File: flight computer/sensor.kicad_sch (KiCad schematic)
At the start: 131 parts, among them IC1 A3909, J1 Micro_SD_Card_Det1, J12 Conn_01x04, J13 1x3 servo, J14 1x3 servo, J15 arming terminal, J16 arming terminal, J17 H9161TR-ND, J19 Screw_Terminal_01x02, J20 Screw_Terminal_01x02, J3 H9161TR-ND, J4 H9161TR-ND, J5 Screw_Term, J6 1x3 servo, J9 1x3 servo, Q1 IRLML6402, Q3 IRLML6402, Q4 IRLML6402, Q5 IRLML6402, Q6 IRLML6402, Q7 BSS138, Q8 IRLML6402, Q9 IRLML6402, U10 LSM6DS3, U11 BGM220SC12WGA2R, U12 PE4259, U5 LPS22HB, U6 GPS, U7 SX1276, U8 NAND, Y4 32MHz

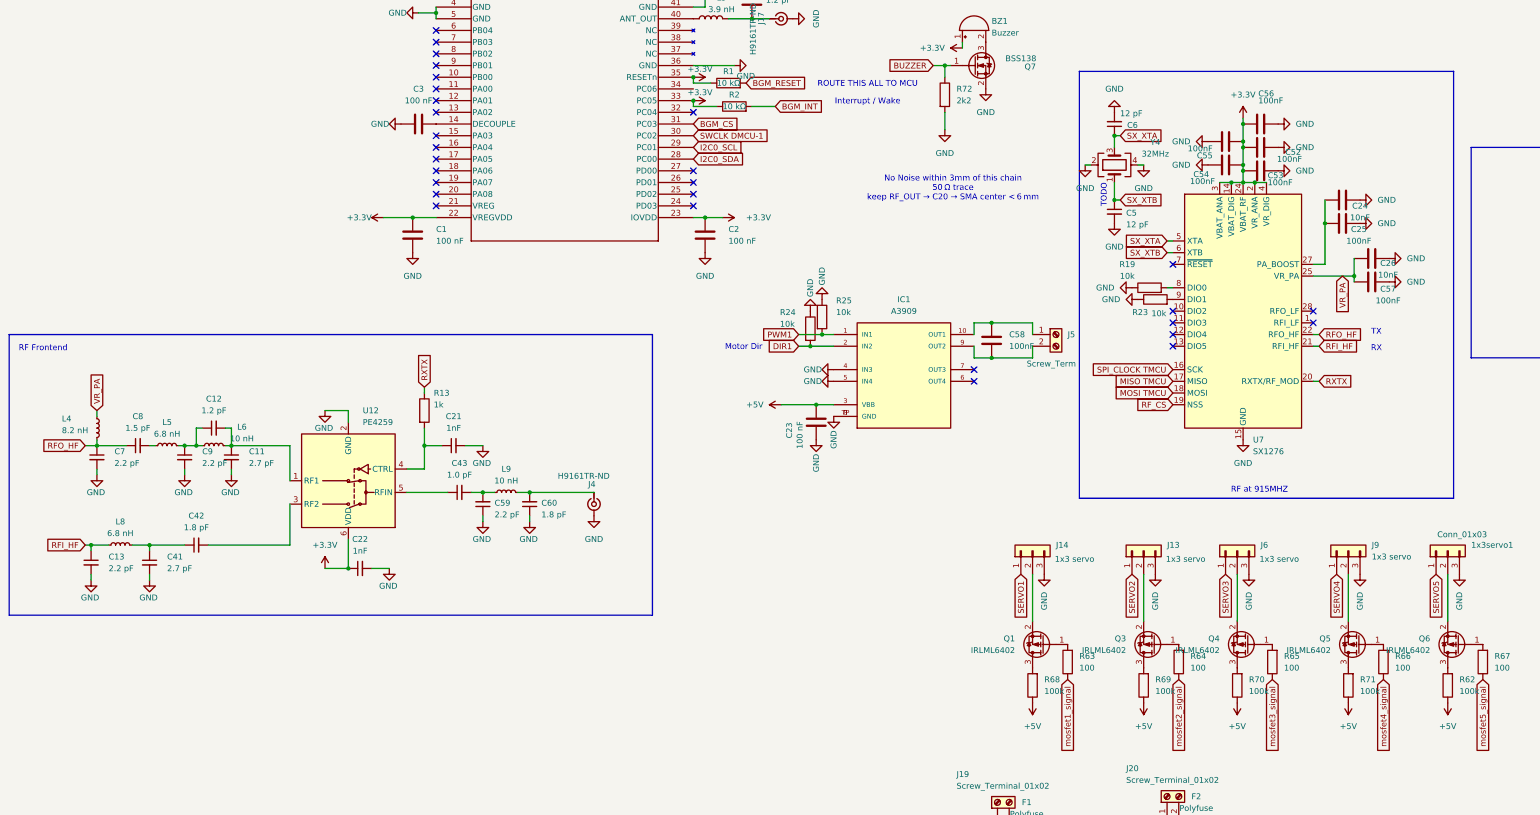
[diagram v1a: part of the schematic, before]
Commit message: Meddy, the PCB is ready for you. The proper RF is setup too on the PCB
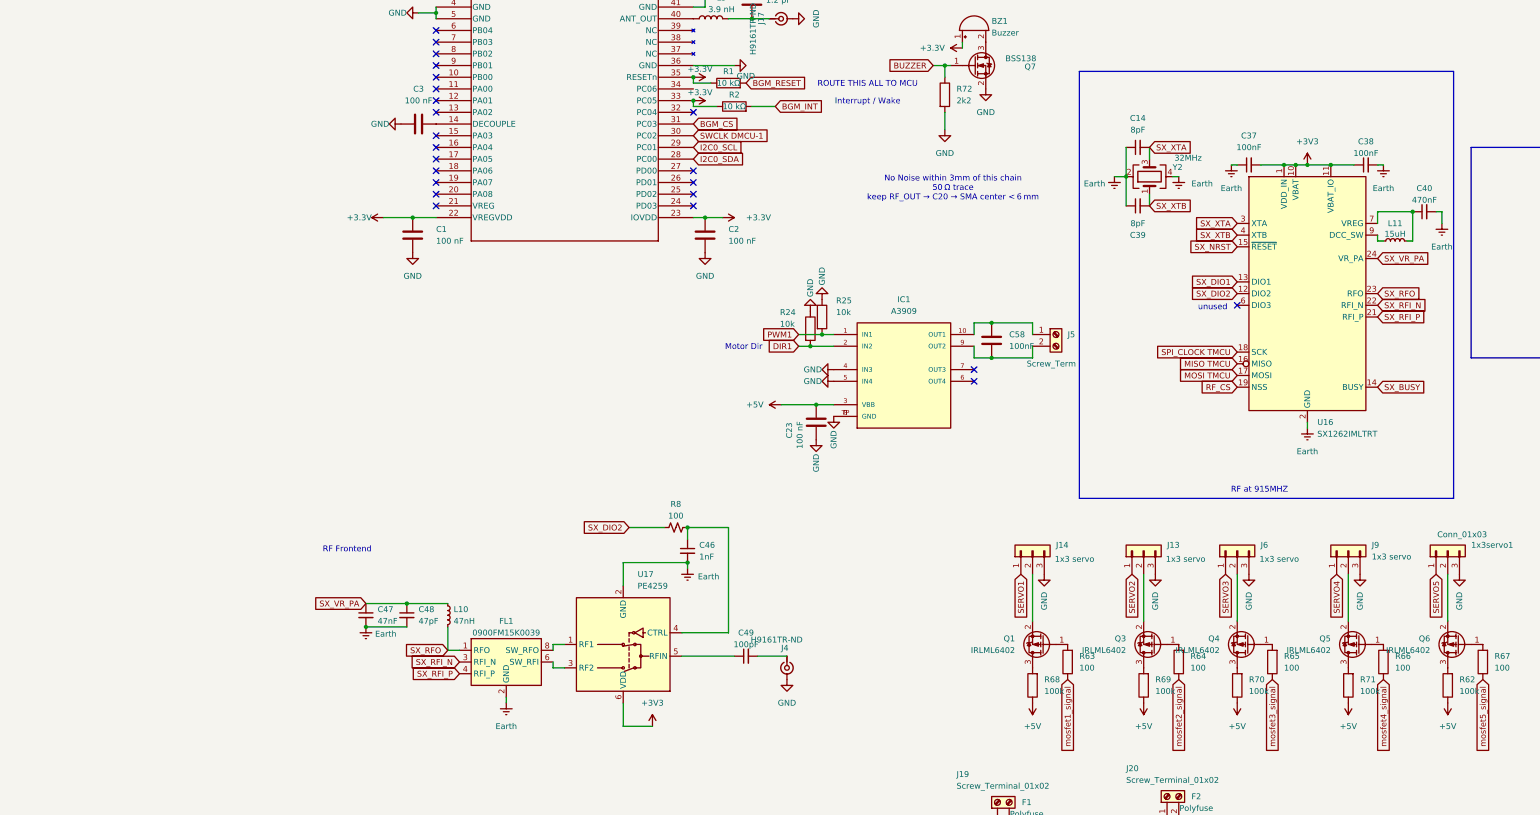
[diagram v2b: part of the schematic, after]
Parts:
- removed C11, C41: 2.7 pF, Capacitor_SMD:C_0603_1608Metric, symbol Device:C_Small
- removed C12: 1.2 pF, Capacitor_SMD:C_0603_1608Metric, symbol Device:C_Small
- removed C13, C59, C7, C9: 2.2 pF, Capacitor_SMD:C_0603_1608Metric, symbol Device:C_Small
- removed C21, C22: 1nF, Capacitor_SMD:C_0603_1608Metric, symbol Device:C_Small
- removed C24, C26: 10nF, Capacitor_SMD:C_0603_1608Metric, symbol Device:C
- removed C25, C52, C53, C54, C55, C56, C57: 100nF, Capacitor_SMD:C_0603_1608Metric, symbol Device:C
- removed C42, C60: 1.8 pF, Capacitor_SMD:C_0603_1608Metric, symbol Device:C_Small
- removed C43: 1.0 pF, Capacitor_SMD:C_0603_1608Metric, symbol Device:C_Small
- removed C5, C6: 12 pF, Capacitor_SMD:C_0603_1608Metric, symbol Device:C_Small
- removed C8: 1.5 pF, Capacitor_SMD:C_0603_1608Metric, symbol Device:C_Small
- removed L4: 8.2 nH, Inductor_SMD:L_0603_1608Metric, symbol Device:L_Small
- removed L5, L8: 6.8 nH, Inductor_SMD:L_0603_1608Metric, symbol Device:L_Small
- removed L6, L9: 10 nH, Inductor_SMD:L_0603_1608Metric, symbol Device:L_Small
- removed R13: 1k, Resistor_SMD:R_0603_1608Metric, symbol Device:R
- removed R19, R23: 10k, Resistor_SMD:R_0603_1608Metric, symbol Device:R
- removed U12: PE4259, Package_TO_SOT_SMD:SOT-363_SC-70-6, symbol RF_Switch:BGS12WN6E6327
- removed U7: SX1276, Package_DFN_QFN:QFN-28-1EP_6x6mm_P0.65mm_EP4.8x4.8mm, symbol RF:SX1276
- removed Y4: 32MHz, Crystal:Crystal_SMD_Abracon_ABM10-4Pin_2.5x2.0mm, symbol Device:Crystal_GND24
- added C14, C39: 8pF, Capacitor_SMD:C_0603_1608Metric, symbol Device:C_Small
- added C37, C38: 100nF, Capacitor_SMD:C_0603_1608Metric, symbol Device:C_Small
- added C40: 470nF, Capacitor_SMD:C_0603_1608Metric, symbol Device:C_Small
- added C46: 1nF, Capacitor_SMD:C_0603_1608Metric, symbol Device:C_Small
- added C47: 47nF, Capacitor_SMD:C_0603_1608Metric, symbol Device:C_Small
- added C48: 47pF, Capacitor_SMD:C_0603_1608Metric, symbol Device:C_Small
- added C49: 100pF, Capacitor_SMD:C_0603_1608Metric, symbol Device:C_Small
- added FL1: 0900FM15K0039, RF_Converter:Balun_Johanson_0900FM15K0039, symbol Filter:0900FM15K0039
- added L10: 47nH, Inductor_SMD:L_0603_1608Metric, symbol Device:L_Small
- added L11: 15uH, Inductor_SMD:L_0805_2012Metric, symbol Device:L_Small
- added R8: 100, Resistor_SMD:R_0603_1608Metric, symbol Device:R_Small_US
- added U16: SX1262IMLTRT, Package_DFN_QFN:QFN-24-1EP_4x4mm_P0.5mm_EP2.6x2.6mm, symbol RF:SX1262IMLTRT
- added U17: PE4259, Package_TO_SOT_SMD:SOT-363_SC-70-6, symbol RF_Switch_Extended:PE4259
- added Y2: 32MHz, Crystal:Crystal_SMD_3225-4Pin_3.2x2.5mm, symbol Device:Crystal_GND24
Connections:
- net MISO TMCU: now also U16.16 (MISO)
- net MOSI TMCU: now also U16.17 (MOSI)
- net RF_CS: now also U16.19 (NSS)
- net SPI_CLOCK TMCU: now also U16.18 (SCK)
- net SX_XTA: now also C14.2, U16.3 (XTA), Y2.3
- net SX_XTB: now also C39.2, U16.4 (XTB), Y2.1
- net at J4.1 (In): now also C49.2
- new net: C49.1, U17.5 (RFIN)
- new net: FL1.6 (SW_RFI), U17.3 (RF2)
- new net: FL1.8 (SW_RFO), U17.1 (RF1)
- new net: C46.1, R8.2, U17.4 (CTRL)
- new net: L11.1, U16.9 (DCC_SW)
- new net: C40.1, L11.2, U16.7 (VREG)
- new net +3V3: C37.2, C38.1, U16.1 (VDD_IN), U16.10 (VBAT), U16.11 (VBAT_IO), U17.6 (VDD)
- new net Earth: C14.1, C37.1, C38.2, C39.1, C40.2, C46.2, C47.2, C48.2, FL1.10 (GND), FL1.2 (GND), FL1.5 (GND), FL1.7 (GND), FL1.9 (GND), U16.2 (GND), U16.20 (GND), U16.25 (GND), U16.5 (GND), U16.8 (GND), U17.2 (GND), Y2.2, Y2.4
- new net SX_BUSY: U16.14 (BUSY)
- new net SX_DIO1: U16.13 (DIO1)
- new net SX_DIO2: R8.1, U16.12 (DIO2)
- new net SX_NRST: U16.15 (~{RESET})
- new net SX_RFI_N: FL1.3 (RFI_N), U16.22 (RFI_N)
- new net SX_RFI_P: FL1.4 (RFI_P), U16.21 (RFI_P)
- new net SX_RFO: FL1.1 (RFO), L10.2, U16.23 (RFO)
- new net SX_VR_PA: C47.1, C48.1, L10.1, U16.24 (VR_PA)
- no-connect marks 47 -> 41
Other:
- note added: "unused"
- note removed: "RX"
- note removed: "TODO"
- note removed: "TX"
- moved on the sheet: J4

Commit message: schematic stuff
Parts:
- removed BZ1: Buzzer, Buzzer_Beeper:MagneticBuzzer_PUI_AT-0927-TT-6-R, symbol Device:Buzzer
- added BZ2: Buzzer, MLT-8530_JHE, symbol SMD_BUZZ:MLT-8530
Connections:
- net +3.3V: now also BZ2.2
- net at Q7.3 (D): now also BZ2.1
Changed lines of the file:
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@@
 	(wire
 		(pts
-			(xy 30.48 96.52) (xy 30.48 97.79)
+			(xy 10.16 88.9) (xy 10.16 90.17)
 		)
 		(stroke
@@
 	(wire
 		(pts
+			(xy 35.56 88.9) (xy 35.56 96.52)
+		)
+		(stroke
+			(width 0)
+			(type default)
+		)
+	)
+	(wire
+		(pts
 			(xy -5.08 162.56) (xy -2.54 162.56)
 		)
@@
 	)
 	(symbol
-		(lib_id "Device:Buzzer")
-		(at 33.02 93.98 90)
-		(unit 1)
-		(exclude_from_sim no)
-		(in_bom yes)
-		(on_board yes)
-		(dnp no)
-		(fields_autoplaced yes)
-		(property "Reference" "BZ1"
-			(at 36.83 91.9548 90)
-			(effects
-				(font
-					(size 1.27 1.27)
-				)
-				(justify right)
-			)
-		)
-		(property "Value" "Buzzer"
-			(at 36.83 94.4948 90)
-			(effects
-				(font
-					(size 1.27 1.27)
-				)
-				(justify right)
-			)
-		)
-		(property "Footprint" "Buzzer_Beeper:MagneticBuzzer_PUI_AT-0927-TT-6-R"
-			(at 30.48 94.615 90)
-			(effects
-				(font
-					(size 1.27 1.27)
-				)
-				(hide yes)
-			)
-		)
-		(property "Datasheet" "~"
-			(at 30.48 94.615 90)
-			(effects
-				(font
-					(size 1.27 1.27)
-				)
-				(hide yes)
-			)
-		)
-		(property "Description" "Buzzer, polarized"
-			(at 33.02 93.98 0)
-			(effects
-				(font
-					(size 1.27 1.27)
-				)
-				(hide yes)
-			)
-		)
-		(pin "1"
-		)
-		(pin "2"
-		)
-		(instances
-			(project "horizon"
-				(path "/78d9c2f3-deae-418a-8c21-4820ea8fc57f/8017925a-458a-4a0a-8733-ba805a96612a"
-					(reference "BZ1")
-					(unit 1)
-				)
-			)
-		)
-	)
-	(symbol
 		(lib_id "Transistor_FET:IRLML6402")
 		(at 77.47 271.78 180)
@@
 	)
 	(symbol
+		(lib_id "SMD_BUZZ:MLT-8530")
+		(at 35.56 88.9 180)
+		(unit 1)
+		(exclude_from_sim no)
+		(in_bom yes)
+		(on_board yes)
+		(dnp no)
+		(fields_autoplaced yes)
+		(property "Reference" "BZ2"
+			(at 22.86 81.28 0)
+			(effects
+				(font
+					(size 1.27 1.27)
+				)
+			)
+		)
+		(property "Value" "Buzzer"
+			(at 22.86 83.82 0)
+			(effects
+				(font
+					(size 1.27 1.27)
+				)
+			)
+		)
+		(property "Footprint" "MLT-8530_JHE"
+			(at 35.56 88.9 0)
+			(effects
+				(font
+					(size 1.27 1.27)
+					(italic yes)
+				)
+				(hide yes)
+			)
+		)
+		(property "Datasheet" "MLT-8530"
+			(at 35.56 88.9 0)
+			(effects
+				(font
+					(size 1.27 1.27)
+					(italic yes)
+				)
+				(hide yes)
+			)
+		)
+		(property "Description" "Buzzer, polarized"
+			(at 35.56 88.9 0)
+			(effects
+				(font
+					(size 1.27 1.27)
+				)
+				(hide yes)
+			)
+		)
+		(pin "1"
+		)
+		(pin "2"
+		)
+		(instances
+			(project "horizon"
+				(path "/78d9c2f3-deae-418a-8c21-4820ea8fc57f/8017925a-458a-4a0a-8733-ba805a96612a"
+					(reference "BZ2")
+					(unit 1)
+				)
+			)
+		)
+	)
+	(symbol
 		(lib_id "power:GND")
 		(at -19.05 101.6 90)
@@
 	(symbol
 		(lib_id "power:+3.3V")
-		(at 30.48 97.79 90)
+		(at 10.16 90.17 90)
 		(unit 1)
 		(exclude_from_sim no)
@@
 		(on_board yes)
 		(dnp no)
-		(fields_autoplaced yes)
 		(property "Reference" "#PWR0120"
-			(at 34.29 97.79 0)
+			(at 13.97 90.17 0)
 			(effects
 				(font
@@
 		)
 		(property "Value" "+3.3V"
-			(at 26.67 97.7899 90)
+			(at 13.97 92.456 90)
 			(effects
 				(font
@@
 		)
 		(property "Footprint" ""
-			(at 30.48 97.79 0)
+			(at 10.16 90.17 0)
 			(effects
 				(font
@@
 		)
 		(property "Datasheet" ""
-			(at 30.48 97.79 0)
+			(at 10.16 90.17 0)
 			(effects
 				(font
@@
 		)
 		(property "Description" "Power symbol creates a global label with name \"+3.3V\""
-			(at 30.48 97.79 0)
+			(at 10.16 90.17 0)
 			(effects
 				(font

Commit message: finished power stuff
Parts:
- BZ2: footprint MLT-8530_JHE -> (none)
- J17, J3, J4: footprint U.FL:HRS_U.FL-R-SMT_01_ -> U.FL-R-SMT_01_:HRS_U.FL-R-SMT_01_
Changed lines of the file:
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@@
 			)
 		)
-		(property "Footprint" "U.FL:HRS_U.FL-R-SMT_01_"
+		(property "Footprint" "U.FL-R-SMT_01_:HRS_U.FL-R-SMT_01_"
 			(at 114.3 49.53 0)
 			(effects
@@
 			)
 		)
-		(property "Footprint" "U.FL:HRS_U.FL-R-SMT_01_"
+		(property "Footprint" "U.FL-R-SMT_01_:HRS_U.FL-R-SMT_01_"
 			(at -7.62 232.41 0)
 			(effects
@@
 			)
 		)
-		(property "Footprint" "U.FL:HRS_U.FL-R-SMT_01_"
+		(property "Footprint" "U.FL-R-SMT_01_:HRS_U.FL-R-SMT_01_"
 			(at -8.89 91.44 0)
 			(effects
@@
 			)
 		)
-		(property "Footprint" "MLT-8530_JHE"
+		(property "Footprint" ""
 			(at 35.56 88.9 0)
 			(effects

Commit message: im getting touched i touch you next
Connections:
- net +5V: now also J16.2 (Pin_2); no longer J16.1 (Pin_1)
- net at D4.1 (K), Q9.2 (S): now also J20.2 (Pin_2); no longer J20.1 (Pin_1)
- net at F2.1: now also J20.1 (Pin_1); no longer J20.2 (Pin_2)
- net at R80.1: now also J16.1 (Pin_1); no longer J16.2 (Pin_2)
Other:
- moved on the sheet: J16, J20
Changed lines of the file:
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@@
 	)
 	(junction
-		(at -15.24 91.44)
+		(at 74.93 265.43)
 		(diameter 0)
 		(color 0 0 0 0)
 	)
 	(junction
-		(at -2.54 162.56)
+		(at -15.24 91.44)
 		(diameter 0)
 		(color 0 0 0 0)
 	)
 	(junction
-		(at 185.42 128.27)
+		(at -2.54 162.56)
 		(diameter 0)
 		(color 0 0 0 0)
 	)
 	(junction
-		(at 74.93 265.43)
+		(at 185.42 128.27)
 		(diameter 0)
 		(color 0 0 0 0)
@@
 	(wire
 		(pts
+			(xy 80.01 262.89) (xy 77.47 265.43)
+		)
+		(stroke
+			(width 0)
+			(type default)
+		)
+	)
+	(wire
+		(pts
 			(xy 106.68 45.72) (xy 106.68 41.91)
 		)
@@
 	(wire
 		(pts
+			(xy 80.01 256.54) (xy 80.01 262.89)
+		)
+		(stroke
+			(width 0)
+			(type default)
+		)
+	)
+	(wire
+		(pts
 			(xy 97.79 -10.16) (xy 91.44 -10.16)
 		)
@@
 	(wire
 		(pts
+			(xy 72.39 287.02) (xy 74.93 287.02)
+		)
+		(stroke
+			(width 0)
+			(type default)
+		)
+	)
+	(wire
+		(pts
 			(xy 93.98 34.29) (xy 104.14 34.29)
 		)
@@
 	(wire
 		(pts
+			(xy 74.93 254) (xy 72.39 256.54)
+		)
+		(stroke
+			(width 0)
+			(type default)
+		)
+	)
+	(wire
+		(pts
 			(xy 224.79 135.89) (xy 227.33 135.89)
 		)
@@
 	(wire
 		(pts
-			(xy 74.93 287.02) (xy 74.93 285.75)
+			(xy 72.39 256.54) (xy 72.39 262.89)
+		)
+		(stroke
+			(width 0)
+			(type default)
+		)
+	)
+	(wire
+		(pts
+			(xy 72.39 289.56) (xy 72.39 287.02)
 		)
 		(stroke
@@
 	(wire
 		(pts
+			(xy 74.93 287.02) (xy 74.93 285.75)
+		)
+		(stroke
+			(width 0)
+			(type default)
+		)
+	)
+	(wire
+		(pts
 			(xy 91.44 -19.05) (xy 91.44 -15.24)
 		)
@@
 	(wire
 		(pts
+			(xy 72.39 262.89) (xy 74.93 265.43)
+		)
+		(stroke
+			(width 0)
+			(type default)
+		)
+	)
+	(wire
+		(pts
 			(xy -83.82 90.17) (xy -83.82 91.44)
 		)
@@
 	(wire
 		(pts
+			(xy 77.47 254) (xy 80.01 256.54)
+		)
+		(stroke
+			(width 0)
+			(type default)
+		)
+	)
+	(wire
+		(pts
 			(xy 34.29 278.13) (xy 30.48 281.94)
 		)
@@
 	(symbol
 		(lib_id "Connector:Screw_Terminal_01x02")
-		(at 74.93 260.35 90)
+		(at 77.47 259.08 270)
 		(unit 1)
 		(exclude_from_sim no)
@@
 		(dnp no)
 		(property "Reference" "J20"
-			(at 66.04 254.254 90)
+			(at 86.36 265.176 90)
 			(effects
 				(font
@@
 		)
 		(property "Value" "Screw_Terminal_01x02"
-			(at 66.04 256.794 90)
+			(at 86.36 262.636 90)
 			(effects
 				(font
@@
 		)
 		(property "Footprint" "TerminalBlock_Phoenix:TerminalBlock_Phoenix_MPT-0,5-2-2.54_1x02_P2.54mm_Horizontal"
-			(at 74.93 260.35 0)
+			(at 77.47 259.08 0)
 			(effects
 				(font
@@
 		)
 		(property "Datasheet" "~"
-			(at 74.93 260.35 0)
+			(at 77.47 259.08 0)
 			(effects
 				(font
@@
 		)
 		(property "Description" "Generic screw terminal, single row, 01x02, script generated (kicad-library-utils/schlib/autogen/connector/)"
-			(at 74.93 260.35 0)
+			(at 77.47 259.08 0)
 			(effects
 				(font
@@
 	(symbol
 		(lib_id "power:+5V")
-		(at 74.93 289.56 180)
+		(at 72.39 292.1 180)
 		(unit 1)
 		(exclude_from_sim no)
@@
 		(fields_autoplaced yes)
 		(property "Reference" "#PWR0177"
-			(at 74.93 285.75 0)
+			(at 72.39 288.29 0)
 			(effects
 				(font
@@
 		)
 		(property "Value" "+5V"
-			(at 74.93 294.64 0)
+			(at 72.39 297.18 0)
 			(effects
 				(font
@@
 		)
 		(property "Footprint" ""
-			(at 74.93 289.56 0)
+			(at 72.39 292.1 0)
 			(effects
 				(font
@@
 		)
 		(property "Datasheet" ""
-			(at 74.93 289.56 0)
+			(at 72.39 292.1 0)
 			(effects
 				(font
@@
 		)
 		(property "Description" "Power symbol creates a global label with name \"+5V\""
-			(at 74.93 289.56 0)
+			(at 72.39 292.1 0)
 			(effects
 				(font
@@
 	(symbol
 		(lib_id "Connector:Screw_Terminal_01x02")
-		(at 69.85 289.56 180)
+		(at 77.47 289.56 0)
 		(unit 1)
 		(exclude_from_sim no)
@@
 		(dnp no)
 		(property "Reference" "J16"
-			(at 64.262 296.672 90)
+			(at 83.058 282.448 90)
 			(effects
 				(font
@@
 		)
 		(property "Value" "arming terminal"
-			(at 66.294 296.926 90)
+			(at 81.026 282.194 90)
 			(effects
 				(font
@@
 		)
 		(property "Footprint" "TerminalBlock_Phoenix:TerminalBlock_Phoenix_MPT-0,5-2-2.54_1x02_P2.54mm_Horizontal"
-			(at 69.85 289.56 0)
+			(at 77.47 289.56 0)
 			(effects
 				(font
@@
 		)
 		(property "Datasheet" "~"
-			(at 69.85 289.56 0)
+			(at 77.47 289.56 0)
 			(effects
 				(font
@@
 		)
 		(property "Description" "Generic screw terminal, single row, 01x02, script generated (kicad-library-utils/schlib/autogen/connector/)"
-			(at 69.85 289.56 0)
+			(at 77.47 289.56 0)
 			(effects
 				(font

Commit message: daily commit
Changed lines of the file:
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@@
-	(wire
-		(pts
-			(xy 135.89 -19.05) (xy 135.89 -15.24)
-		)
-		(stroke
-			(width 0)
-			(type default)
-		)
-	)
 	(wire
 		(pts
@@
 	(symbol
 		(lib_id "power:GND")
-		(at 135.89 -19.05 180)
+		(at 135.89 -15.24 180)
 		(unit 1)
 		(exclude_from_sim no)
@@
 		(fields_autoplaced yes)
 		(property "Reference" "#PWR0221"
-			(at 135.89 -25.4 0)
+			(at 135.89 -21.59 0)
 			(effects
 				(font
@@
 		)
 		(property "Value" "GND"
-			(at 135.89 -24.13 0)
+			(at 135.89 -20.32 0)
 			(effects
 				(font
@@
 		)
 		(property "Footprint" ""
-			(at 135.89 -19.05 0)
+			(at 135.89 -15.24 0)
 			(effects
 				(font
@@
 		)
 		(property "Datasheet" ""
-			(at 135.89 -19.05 0)
+			(at 135.89 -15.24 0)
 			(effects
 				(font
@@
 		)
 		(property "Description" "Power symbol creates a global label with name \"GND\" , ground"
-			(at 135.89 -19.05 0)
-			(effects
-				(font
+			(at 135.89 -15.24 0)
+			(effects
+				(font

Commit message: more wiring kms
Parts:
- removed C23: 100 nF, Capacitor_SMD:C_0603_1608Metric, symbol Device:C
- removed C58: 100nF, Capacitor_SMD:C_0603_1608Metric, symbol Device:C
- removed IC1: A3909, A3909:MSOP10-PAD, symbol A3909:A3909
- removed R24, R25: 10k, Resistor_SMD:R_0603_1608Metric, symbol Device:R
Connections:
- no-connect marks 41 -> 39
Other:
- note removed: "Motor Dir"

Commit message: wiring fml
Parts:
- removed Q1, Q3, Q4, Q5, Q6: IRLML6402, Package_TO_SOT_SMD:SOT-23, symbol Transistor_FET:IRLML6402
- removed R62, R68, R69, R70, R71: 100k, Resistor_SMD:R_0603_1608Metric, symbol Device:R
- removed R63, R64, R65, R66, R67: 100, Resistor_SMD:R_0603_1608Metric, symbol Device:R
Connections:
- net +5V: now also 1x3servo1.2 (Pin_2), J13.2 (Pin_2), J14.2 (Pin_2), J6.2 (Pin_2), J9.2 (Pin_2)
- net at D4.1 (K), Q9.2 (S): no longer J20.2 (Pin_2)
- net at J20.1 (Pin_1): no longer F2.1
